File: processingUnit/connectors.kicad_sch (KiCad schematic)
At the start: 27 parts, among them J101 Conn_01x05, J301 Conn_01x10, J304 Conn_01x04, J309 Conn_01x02, J310 Conn_01x06, J311 Conn_01x03, J312 Conn_01x03, SW304 ENC RST

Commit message: l3 might redo
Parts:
- renumbered C101 to C201, C102 to C202, C103 to C203, C104 to C204, C319 to C205, FB101 to FB201, FB102 to FB202, H301 to H201, H305 to H202, H309 to H203, H302 to H204, H306 to H205, H310 to H206, H303 to H207, H307 to H208, H311 to H209, H304 to H210, H308 to H211, H312 to H212, J310 to J201, J101 to J202, J311 to J203, J309 to J204, J312 to J205, J301 to J206, J304 to J207, SW304 to SW202

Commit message: l3 might redo
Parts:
- renumbered C201 to C101, C202 to C102, C203 to C103, C204 to C104, C205 to C105, FB201 to FB101, FB202 to FB102, H201 to H101, H202 to H102, H203 to H103, H204 to H104, H205 to H105, H206 to H106, H207 to H107, H208 to H108, H209 to H109, H210 to H110, H211 to H111, H212 to H112, J201 to J101, J202 to J102, J203 to J103, J204 to J104, J205 to J105, J206 to J106, J207 to J107, SW202 to SW101

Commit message: drivers
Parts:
- C105: value C -> 0u1
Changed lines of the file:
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@@
 			)
 		)
-		(property "Value" "C"
+		(property "Value" "0u1"
 			(at 171.45 153.6699 0)
 			(effects

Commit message: l3 routing
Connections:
- net +3V3: no longer J101.2 (Pin_2)
- net +3V3 FILT: now also J101.2 (Pin_2)
- net +5V: no longer J101.1 (Pin_1)
- net +5V FILT: now also J101.1 (Pin_1)

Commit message: switch position
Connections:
- net GATE RX: no longer names the net of J106.2 (Pin_2)
- net GATE TX renamed FLAG 2
- no-connect marks 2 -> 3
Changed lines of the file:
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@@
+	)
+	(no_connect
+		(at 91.44 161.29)
 	)
 	(no_connect
@@
 		(pts
 			(xy 48.26 102.87) (xy 48.26 96.52)
-		)
-		(stroke
-			(width 0)
-			(type default)
-		)
-	)
-	(wire
-		(pts
-			(xy 91.44 161.29) (xy 93.98 161.29)
 		)
 		(stroke
@@
 		)
 	)
-	(hierarchical_label "GATE TX"
-		(shape bidirectional)
-		(at 93.9303 158.75 0)
-		(effects
-			(font
-				(size 1.27 1.27)
-			)
-			(justify left)
-		)
-	)
-	(hierarchical_label "GATE RX"
-		(shape bidirectional)
-		(at 93.98 161.29 0)
-		(effects
-			(font
+	(hierarchical_label "FLAG 2"
+		(shape output)
+		(at 93.98 158.75 0)
+		(effects
+			(font

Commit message: step
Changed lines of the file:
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@@
 	)
 	(hierarchical_label "L3 TX"
-		(shape output)
+		(shape input)
 		(at 49.53 107.95 0)
 		(effects

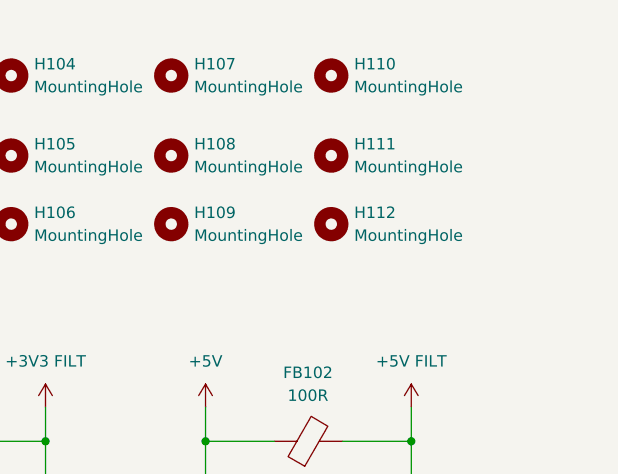
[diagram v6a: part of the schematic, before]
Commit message: simple routing
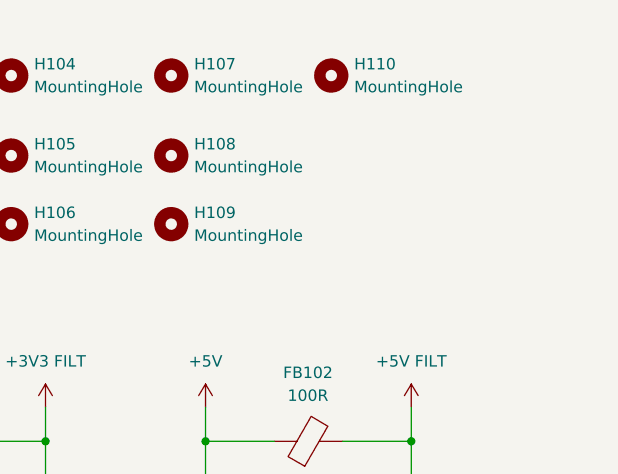
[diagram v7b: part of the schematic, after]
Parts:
- removed H111, H112: MountingHole, MountingHole:MountingHole_3.2mm_M3_Pad_Via, symbol Mechanical:MountingHole
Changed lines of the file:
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@@
-	)
-	(symbol
-		(lib_id "Mechanical:MountingHole")
-		(at 147.32 64.77 0)
-		(unit 1)
-		(exclude_from_sim no)
-		(in_bom yes)
-		(on_board yes)
-		(dnp no)
-		(fields_autoplaced yes)
-		(property "Reference" "H111"
-			(at 149.86 63.4999 0)
-			(effects
-				(font
-					(size 1.27 1.27)
-				)
-				(justify left)
-			)
-		)
-		(property "Value" "MountingHole"
-			(at 149.86 66.0399 0)
-			(effects
-				(font
-					(size 1.27 1.27)
-				)
-				(justify left)
-			)
-		)
-		(property "Footprint" "MountingHole:MountingHole_3.2mm_M3_Pad_Via"
-			(at 147.32 64.77 0)
-			(effects
-				(font
-					(size 1.27 1.27)
-				)
-				(hide yes)
-			)
-		)
-		(property "Datasheet" "~"
-			(at 147.32 64.77 0)
-			(effects
-				(font
-					(size 1.27 1.27)
-				)
-				(hide yes)
-			)
-		)
-		(property "Description" "Mounting Hole without connection"
-			(at 147.32 64.77 0)
-			(effects
-				(font
-					(size 1.27 1.27)
-				)
-				(hide yes)
-			)
-		)
-		(instances
-			(project "l3"
-				(path "/1b1408da-cc6a-469f-a506-e797247b3ac8/26fa24e2-dd9a-49a9-9a0e-c48ef9d66c8d"
-					(reference "H111")
-					(unit 1)
-				)
-			)
-		)
 	)
 	(symbol
@@
 					(unit 1)
 				)
-			)
-		)
-	)
-	(symbol
-		(lib_id "Mechanical:MountingHole")
-		(at 147.32 72.39 0)
-		(unit 1)
-		(exclude_from_sim no)
-		(in_bom yes)
-		(on_board yes)
-		(dnp no)
-		(fields_autoplaced yes)
-		(property "Reference" "H112"
-			(at 149.86 71.1199 0)
-			(effects
-				(font
-					(size 1.27 1.27)
-				)
-				(justify left)
-			)
-		)
-		(property "Value" "MountingHole"
-			(at 149.86 73.6599 0)
-			(effects
-				(font
-					(size 1.27 1.27)
-				)
-				(justify left)
-			)
-		)
-		(property "Footprint" "MountingHole:MountingHole_3.2mm_M3_Pad_Via"
-			(at 147.32 72.39 0)
-			(effects
-				(font
-					(size 1.27 1.27)
-				)
-				(hide yes)
-			)
-		)
-		(property "Datasheet" "~"
-			(at 147.32 72.39 0)
-			(effects
-				(font
-					(size 1.27 1.27)
-				)
-				(hide yes)
-			)
-		)
-		(property "Description" "Mounting Hole without connection"
-			(at 147.32 72.39 0)
-			(effects
-				(font
-					(size 1.27 1.27)
-				)
-				(hide yes)
-			)
-		)
-		(instances
-			(project "l3"
-				(path "/1b1408da-cc6a-469f-a506-e797247b3ac8/26fa24e2-dd9a-49a9-9a0e-c48ef9d66c8d"
-					(reference "H112")
-					(unit 1)
-				)

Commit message: nightmare fuel
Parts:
- added H111, H112, H113, H114: MountingHole, MountingHole:MountingHole_3.2mm_M3_Pad_Via, symbol Mechanical:MountingHole
